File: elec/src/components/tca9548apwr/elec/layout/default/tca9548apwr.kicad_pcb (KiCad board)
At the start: 2 copper layers, 225.7 x 100.8 mm, 20 parts

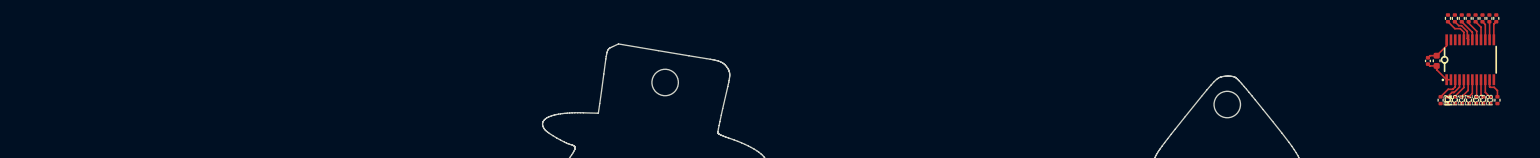
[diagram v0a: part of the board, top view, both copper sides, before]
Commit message: use linked modules, remove local cache
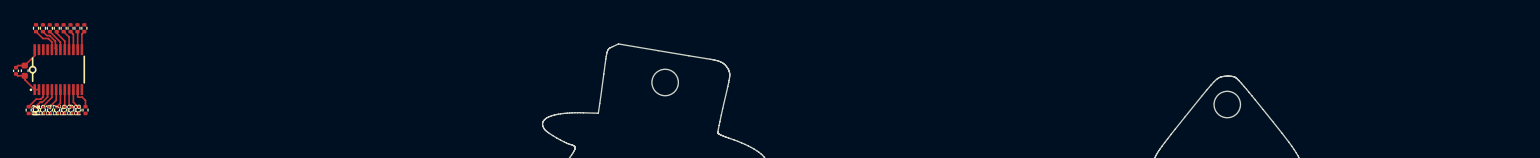
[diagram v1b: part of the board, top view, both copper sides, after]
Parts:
- moved C2 213.7 mm to (-20.7, 53.8)
- moved R11 213.7 mm to (-11.7, 47.4)
- moved R13 213.7 mm to (-13.8, 47.4)
- moved R15 213.7 mm to (-15.9, 47.4)
- moved R16 213.7 mm to (-19.0, 47.4)
- moved R5 213.7 mm to (-16.9, 59.8)
- moved R8 213.7 mm to (-11.5, 59.8)
- moved C1 213.7 mm to (-22.1, 53.8)
- moved R1 213.7 mm to (-20.1, 59.8)
- moved R10 213.7 mm to (-12.8, 47.4)
- moved R12 213.7 mm to (-14.9, 47.4)
- moved R14 213.7 mm to (-16.9, 47.4)
- moved R17 213.7 mm to (-18.0, 47.4)
- moved R2 213.7 mm to (-18.0, 59.8)
- moved R3 213.7 mm to (-19.1, 59.8)
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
